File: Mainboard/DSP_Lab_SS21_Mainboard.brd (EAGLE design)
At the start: 160 x 120 mm, 60 parts, among them IC1 TL072CD, IC2 LM386M-1_NOPB, J1 USB3076, J2 640455-5, J3 640455-3, J4 640455-4, J5 640455-4, J6 SJ-3523-SMT-TR, J7 640455-2, J8 929850-01-06-RB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

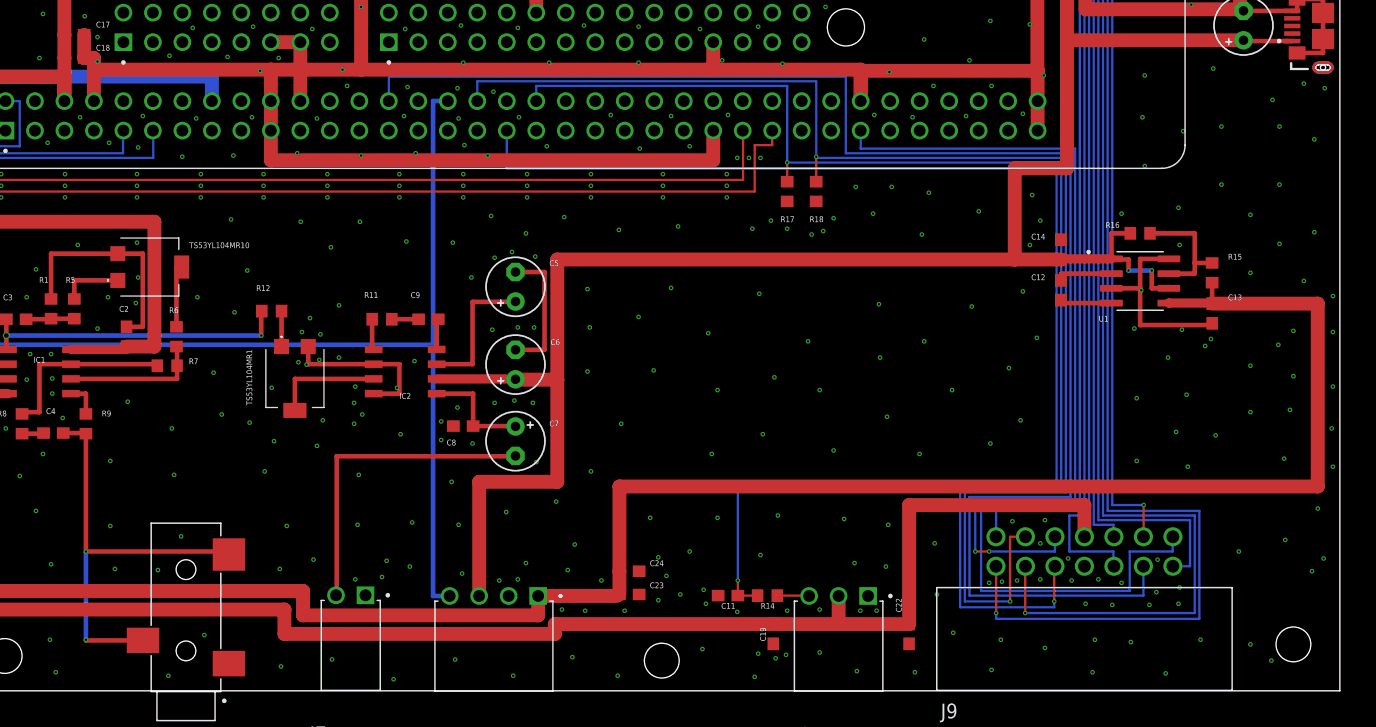
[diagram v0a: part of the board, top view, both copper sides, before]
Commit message: Production data for ordering Mainboard, Keys, UI and EQ at JLCPCB
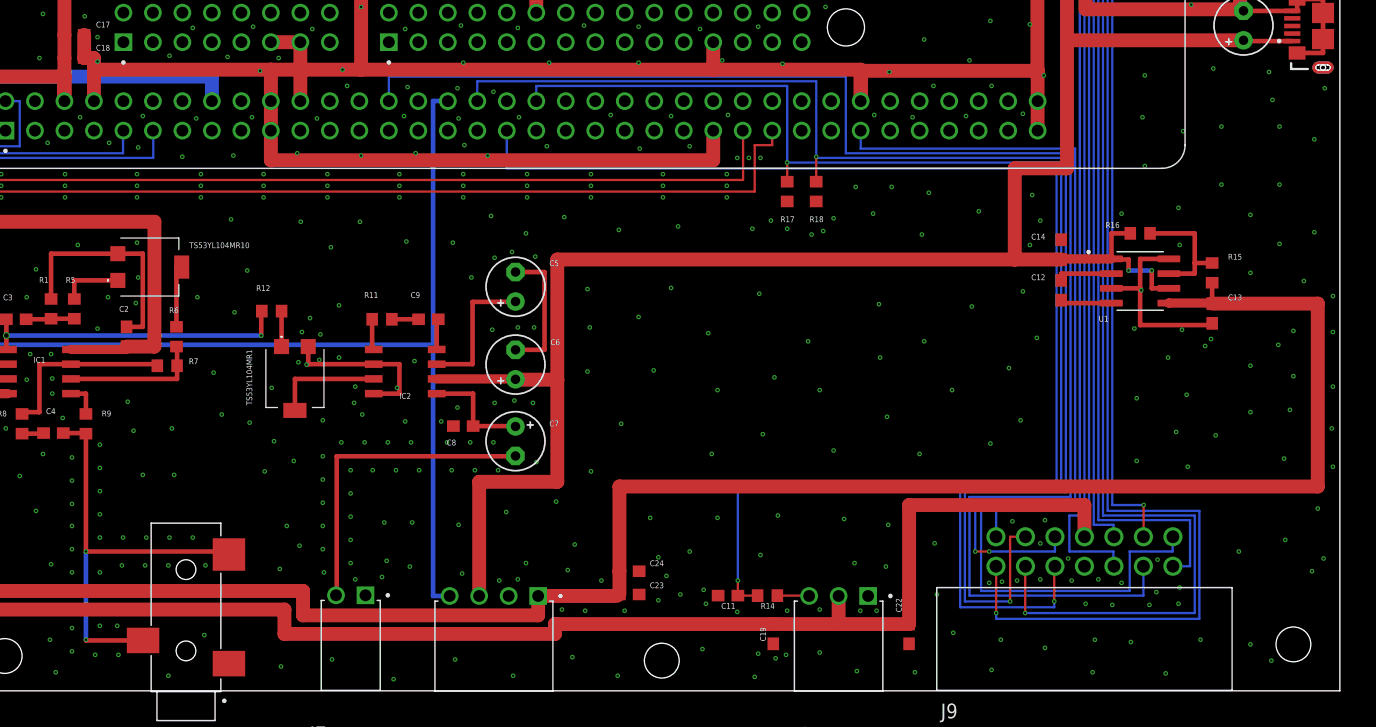
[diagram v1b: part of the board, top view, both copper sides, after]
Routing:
- net GND: vias 839 -> 881
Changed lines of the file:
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@@
 <setting verticaltext="up"/>
 </settings>
-<grid distance="1" unitdist="mm" unit="mm" style="lines" multiple="1" display="yes" altdistance="0.025" altunitdist="mm" altunit="mm"/>
+<grid distance="0.1" unitdist="mm" unit="mm" style="lines" multiple="1" display="yes" altdistance="0.025" altunitdist="mm" altunit="mm"/>
 <layers>
 <layer number="1" name="Top" color="4" fill="1" visible="yes" active="yes"/>
@@
 <via x="44.1" y="25.6" extent="1-16" drill="0.2"/>
 <via x="43.3" y="20.4" extent="1-16" drill="0.2"/>
-<via x="49.1" y="19.8" extent="1-16" drill="0.2"/>
-<via x="49.1" y="14.2" extent="1-16" drill="0.2"/>
-<via x="55.2" y="13.3" extent="1-16" drill="0.2"/>
-<via x="49.5" y="10.5" extent="1-16" drill="0.2"/>
-<via x="53.2" y="10.4" extent="1-16" drill="0.2"/>
+<via x="51.1" y="22.4" extent="1-16" drill="0.2"/>
+<via x="51.9" y="18.6" extent="1-16" drill="0.2"/>
+<via x="52.2" y="13.2" extent="1-16" drill="0.2"/>
+<via x="50.2" y="13.2" extent="1-16" drill="0.2"/>
+<via x="54.2" y="13.2" extent="1-16" drill="0.2"/>
 <via x="63.7" y="10.5" extent="1-16" drill="0.2"/>
-<via x="66.6" y="11.3" extent="1-16" drill="0.2"/>
+<via x="65.4" y="12.5" extent="1-16" drill="0.2"/>
 <via x="64.3" y="14.2" extent="1-16" drill="0.2"/>
 <via x="62.4" y="18.9" extent="1-16" drill="0.2"/>
@@
 <via x="54.4" y="22.6" extent="1-16" drill="0.2"/>
 <via x="58.7" y="23.8" extent="1-16" drill="0.2"/>
-<via x="70.1" y="23" extent="1-16" drill="0.2"/>
-<via x="74.1" y="22.1" extent="1-16" drill="0.2"/>
-<via x="70.5" y="18.6" extent="1-16" drill="0.2"/>
+<via x="71" y="21.4" extent="1-16" drill="0.2"/>
+<via x="74.5" y="23.2" extent="1-16" drill="0.2"/>
+<via x="69.8" y="19" extent="1-16" drill="0.2"/>
 <via x="75.1" y="14.5" extent="1-16" drill="0.2"/>
-<via x="70.4" y="14.3" extent="1-16" drill="0.2"/>
+<via x="72.7" y="14.5" extent="1-16" drill="0.2"/>
 <via x="74.9" y="10.7" extent="1-16" drill="0.2"/>
 <via x="72.9" y="11.2" extent="1-16" drill="0.2"/>
-<via x="78.5" y="18" extent="1-16" drill="0.2"/>
+<via x="82.5" y="19" extent="1-16" drill="0.2"/>
 <via x="79.1" y="14.3" extent="1-16" drill="0.2"/>
 <via x="79.4" y="10.1" extent="1-16" drill="0.2"/>
@@
 <via x="73.8" y="26.1" extent="1-16" drill="0.2"/>
 <via x="75.3" y="28.4" extent="1-16" drill="0.2"/>
-<via x="66.9" y="21.1" extent="1-16" drill="0.2"/>
+<via x="64.9" y="19.8" extent="1-16" drill="0.2"/>
 <via x="66.3" y="32.1" extent="1-16" drill="0.2"/>
 <via x="66" y="28.1" extent="1-16" drill="0.2"/>
@@
 <via x="128.3" y="38.4" extent="1-16" drill="0.2"/>
 <via x="153.7" y="51.9" extent="1-16" drill="0.2"/>
-<via x="151.9" y="52.3" extent="1-16" drill="0.2"/>
+<via x="148.9" y="53.3" extent="1-16" drill="0.2"/>
 <via x="151.9" y="62.4" extent="1-16" drill="0.2"/>
 <via x="154.1" y="62.4" extent="1-16" drill="0.2"/>
@@
 <via x="79" y="24.4" extent="1-16" drill="0.2"/>
 <via x="77.6" y="23.2" extent="1-16" drill="0.2"/>
-<via x="77.6" y="21.6" extent="1-16" drill="0.2"/>
-<via x="80.3" y="21.3" extent="1-16" drill="0.2"/>
+<via x="78.1" y="21.4" extent="1-16" drill="0.2"/>
+<via x="80.1" y="21.4" extent="1-16" drill="0.2"/>
 <via x="70.2" y="26.2" extent="1-16" drill="0.2"/>
 <via x="70.1" y="24.8" extent="1-16" drill="0.2"/>
@@
 <via x="-3.2" y="119" extent="1-16" drill="0.2"/>
 <via x="15.3" y="88.6" extent="1-16" drill="0.2"/>
+<via x="45.8" y="20.1" extent="1-16" drill="0.2"/>
+<via x="45.8" y="18.1" extent="1-16" drill="0.2"/>
+<via x="45.8" y="16.1" extent="1-16" drill="0.2"/>
+<via x="45.8" y="14.2" extent="1-16" drill="0.2"/>
+<via x="45.8" y="12.2" extent="1-16" drill="0.2"/>
+<via x="45.8" y="10.2" extent="1-16" drill="0.2"/>
+<via x="45.8" y="5.4" extent="1-16" drill="0.2"/>
+<via x="45.8" y="3.4" extent="1-16" drill="0.2"/>
+<via x="47.8" y="3.1" extent="1-16" drill="0.2"/>
+<via x="49.8" y="3.1" extent="1-16" drill="0.2"/>
+<via x="48.2" y="5.6" extent="1-16" drill="0.2"/>
+<via x="49.7" y="5.6" extent="1-16" drill="0.2"/>
+<via x="48.2" y="10.2" extent="1-16" drill="0.2"/>
+<via x="48.2" y="13.2" extent="1-16" drill="0.2"/>
+<via x="48.2" y="15.2" extent="1-16" drill="0.2"/>
+<via x="48.2" y="17.2" extent="1-16" drill="0.2"/>
+<via x="48.2" y="19.2" extent="1-16" drill="0.2"/>
+<via x="48.2" y="21.2" extent="1-16" drill="0.2"/>
+<via x="56.2" y="13.2" extent="1-16" drill="0.2"/>
+<via x="50.1" y="10.8" extent="1-16" drill="0.2"/>
+<via x="52.1" y="10.8" extent="1-16" drill="0.2"/>
+<via x="54.1" y="10.8" extent="1-16" drill="0.2"/>
+<via x="57.3" y="10.8" extent="1-16" drill="0.2"/>
+<via x="80.5" y="19" extent="1-16" drill="0.2"/>
+<via x="78.5" y="19" extent="1-16" drill="0.2"/>
+<via x="75.7" y="19" extent="1-16" drill="0.2"/>
+<via x="73.7" y="19" extent="1-16" drill="0.2"/>
+<via x="71.7" y="19" extent="1-16" drill="0.2"/>
+<via x="69.8" y="17" extent="1-16" drill="0.2"/>
+<via x="69.8" y="15" extent="1-16" drill="0.2"/>
+<via x="69.8" y="13" extent="1-16" drill="0.2"/>
+<via x="69.8" y="11" extent="1-16" drill="0.2"/>
+<via x="67.5" y="10.2" extent="1-16" drill="0.2"/>
+<via x="67.4" y="12.2" extent="1-16" drill="0.2"/>
+<via x="67.4" y="14.2" extent="1-16" drill="0.2"/>
+<via x="67.4" y="16.2" extent="1-16" drill="0.2"/>
+<via x="67.4" y="18.2" extent="1-16" drill="0.2"/>
+<via x="67.4" y="20.2" extent="1-16" drill="0.2"/>
+<via x="69" y="21.4" extent="1-16" drill="0.2"/>
+<via x="73" y="21.4" extent="1-16" drill="0.2"/>
+<via x="75" y="21.4" extent="1-16" drill="0.2"/>
+<via x="82.1" y="21.4" extent="1-16" drill="0.2"/>
 </signal>
 <signal name="+5V">

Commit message: Added pictures for EMG and Mainboard for final report
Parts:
- R17, R18, R19: value 1Meg -> 100k
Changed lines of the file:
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@@
 <setting verticaltext="up"/>
 </settings>
-<grid distance="0.1" unitdist="mm" unit="mm" style="lines" multiple="1" display="yes" altdistance="0.025" altunitdist="mm" altunit="mm"/>
+<grid distance="10" unitdist="mm" unit="mm" style="lines" multiple="1" display="yes" altdistance="0.025" altunitdist="mm" altunit="mm"/>
 <layers>
 <layer number="1" name="Top" color="4" fill="1" visible="yes" active="yes"/>
@@
 <text x="69" y="137.5" size="5" layer="48">HEAD</text>
 <text x="72" y="-23" size="5" layer="48">FEET</text>
-<text x="178" y="66" size="5" layer="48">LEFT ARM</text>
+<text x="188" y="66" size="5" layer="48">LEFT ARM</text>
 <text x="-64.25" y="61.925" size="5" layer="48">RIGHT ARM</text>
 <text x="7.5" y="16" size="2" layer="100">EMG</text>
@@
 <attribute name="VALUE" x="129.635" y="38.705" size="0.5" layer="27" rot="R180"/>
 </element>
-<element name="R17" library="rcl" package="R0603" value="1Meg" x="107.4" y="43" smashed="yes" rot="R90">
+<element name="R17" library="rcl" package="R0603" value="100k" x="107.4" y="43" smashed="yes" rot="R90">
 <attribute name="NAME" x="108.035" y="40.865" size="0.5" layer="25" rot="R180"/>
 <attribute name="VALUE" x="108.035" y="41.405" size="0.5" layer="27" rot="R180"/>
 </element>
-<element name="R18" library="rcl" package="R0603" value="1Meg" x="109.9" y="43" smashed="yes" rot="R90">
+<element name="R18" library="rcl" package="R0603" value="100k" x="109.9" y="43" smashed="yes" rot="R90">
 <attribute name="NAME" x="110.535" y="40.865" size="0.5" layer="25" rot="R180"/>
 <attribute name="VALUE" x="110.535" y="41.405" size="0.5" layer="27" rot="R180"/>
 </element>
-<element name="R19" library="rcl" package="R0603" value="1Meg" x="53.8" y="116.6" smashed="yes">
+<element name="R19" library="rcl" package="R0603" value="100k" x="53.8" y="116.6" smashed="yes">
 <attribute name="NAME" x="51.665" y="115.965" size="0.5" layer="25" rot="R90"/>
 <attribute name="VALUE" x="52.205" y="115.965" size="0.5" layer="27" rot="R90"/>
@@
 <wire x1="18.4" y1="2.85" x2="20.4" y2="2.85" width="1.2" layer="1"/>
 <polygon width="0.4" layer="1" spacing="0.2" isolate="0.2" thermals="no">
-<vertex x="-15" y="130"/>
-<vertex x="-15" y="-10"/>
-<vertex x="170" y="-10"/>
-<vertex x="170" y="130"/>
+<vertex x="-65" y="150"/>
+<vertex x="-65" y="-30"/>
+<vertex x="220" y="-30"/>
+<vertex x="220" y="150"/>
 </polygon>
 <polygon width="0.4" layer="16" spacing="0.2" isolate="0.2" thermals="no">
-<vertex x="-10" y="125"/>
-<vertex x="160" y="125"/>
-<vertex x="160" y="-15"/>
-<vertex x="-10" y="-15"/>
+<vertex x="-70" y="155"/>
+<vertex x="230" y="155"/>
+<vertex x="230" y="-35"/>
+<vertex x="-70" y="-35"/>
 </polygon>
 <via x="36.1" y="19.9" extent="1-16" drill="0.2"/>
